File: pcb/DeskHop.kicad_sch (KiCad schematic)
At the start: 12 parts, among them J1 Keyboard In, J2 Debug2, J3 Debug1, J4 Mouse In, U1 Pico Primary, U2 Pico Secondary, U4 ADuM1201BR

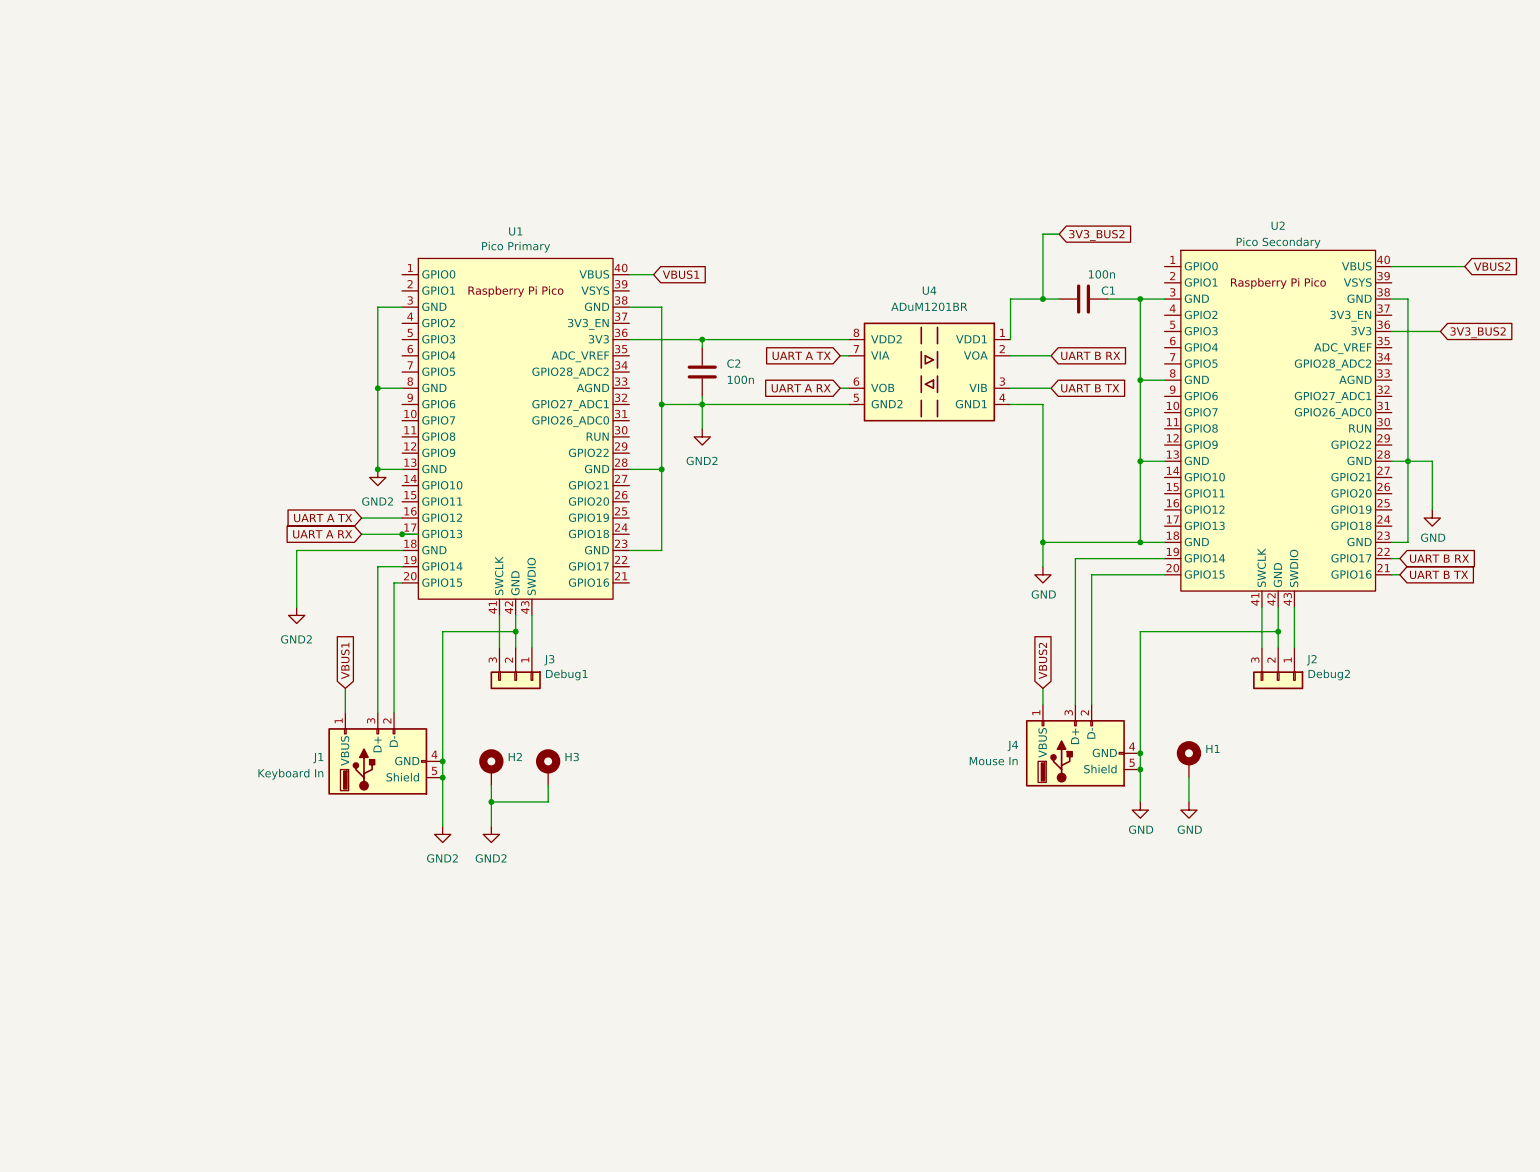
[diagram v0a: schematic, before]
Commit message: Changed design to Type C pico copy
Modifications done to adapt design to Type C version of Pico-copy available in India. Detail changes in PCB Schematics.
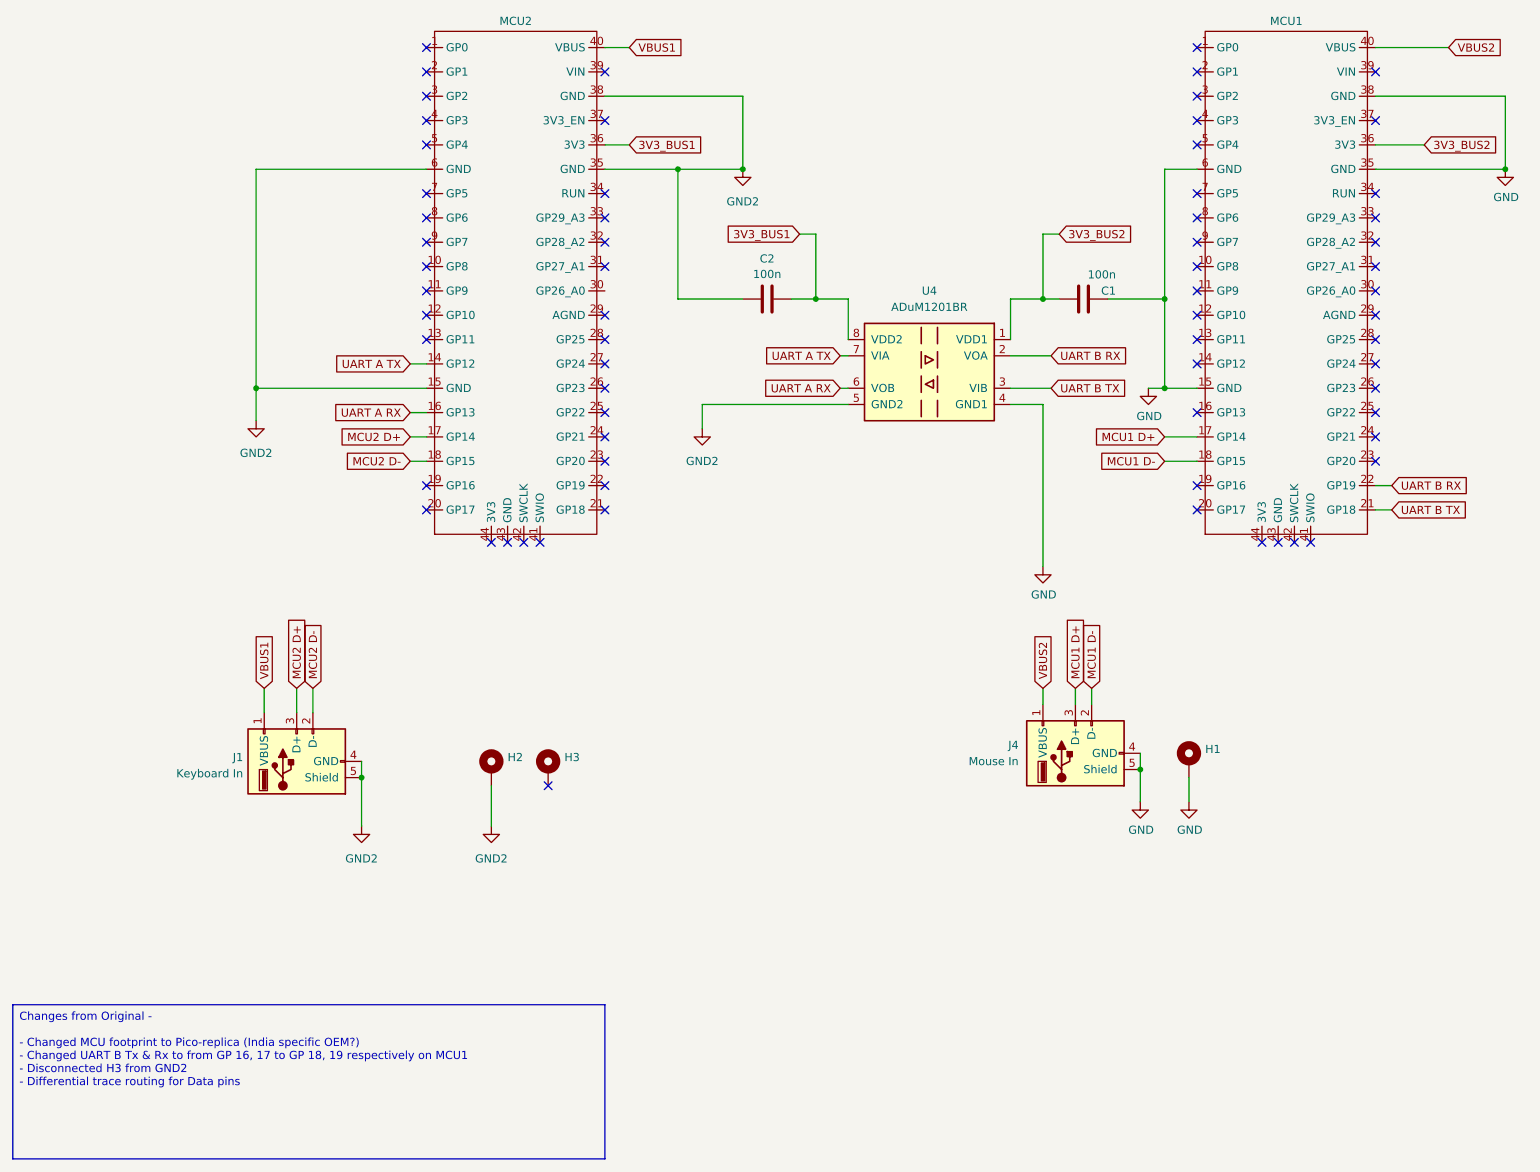
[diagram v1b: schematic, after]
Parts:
- removed J2: Debug2, Connector_PinHeader_2.54mm:PinHeader_1x03_P2.54mm_Vertical, symbol Connector_Generic:Conn_01x03
- removed J3: Debug1, Connector_PinHeader_2.54mm:PinHeader_1x03_P2.54mm_Vertical, symbol Connector_Generic:Conn_01x03
- removed U1: Pico Primary, MCU_RaspberryPi_and_Boards:RPi_Pico_SMD_Nohole, symbol MCU_RaspberryPi_and_Boards:Pico
- removed U2: Pico Secondary, MCU_RaspberryPi_and_Boards:RPi_Pico_SMD_Nohole, symbol MCU_RaspberryPi_and_Boards:Pico
- added MCU1, MCU2: ~, OEM_like:Pico_like, symbol OEM-like:Pico_like_Umang
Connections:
- net 3V3_BUS2: now also MCU1.36 (3V3)
- net GND: now also MCU1.15 (GND), MCU1.35 (GND), MCU1.38 (GND), MCU1.6 (GND)
- net GND2: now also C2.1, MCU2.15 (GND), MCU2.35 (GND), MCU2.38 (GND), MCU2.6 (GND); no longer C2.2, H3.1
- net UART A RX: now also MCU2.16 (GP13)
- net UART A TX: now also MCU2.14 (GP12)
- net UART B RX: now also MCU1.22 (GP19)
- net UART B TX: now also MCU1.21 (GP18)
- net VBUS1: now also MCU2.40 (VBUS)
- net VBUS2: now also MCU1.40 (VBUS)
- net MCU2 D+: now reaches J1.3 (D+)
- net MCU2 D+: now also MCU2.17 (GP14)
- net MCU2 D-: now reaches J1.2 (D-)
- net MCU2 D-: now also MCU2.18 (GP15)
- net 3V3_BUS1: now reaches U4.8 (VDD2)
- net 3V3_BUS1: now also C2.2, MCU2.36 (3V3); no longer C2.1
- net MCU1 D+: now reaches J4.3 (D+)
- net MCU1 D+: now also MCU1.17 (GP14)
- net MCU1 D-: now reaches J4.2 (D-)
- net MCU1 D-: now also MCU1.18 (GP15)
- no-connect marks 0 -> 68
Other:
- title: DeskHop - Fast Keyboard/Mouse Switching Device -> DeskHop - Fast Keyboard/Mouse Switching Device - Type C
- moved on the sheet: C2, J1

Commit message: reverted back to orignal GPIO for MCU 1
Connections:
- net UART B RX: now also MCU1.20 (GP17); no longer MCU1.22 (GP19)
- net UART B TX: now also MCU1.19 (GP16); no longer MCU1.21 (GP18)
